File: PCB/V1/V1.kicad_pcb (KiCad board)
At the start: 2 copper layers, 19 parts, among them J2 Conn_01x01_Socket, J3 Conn_01x01_Socket, J4 Conn_01x01_Socket, J5 Conn_01x01_Socket, J7 Conn_01x01_Socket, J8 Conn_01x01_Socket, U1 ESP32-DEVKIT-V1, U2 L293D, U3 A4988_STEPPER_MOTOR_DRIVER_CA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, U5 YAAJ_DCDC_StepDown_LM2596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

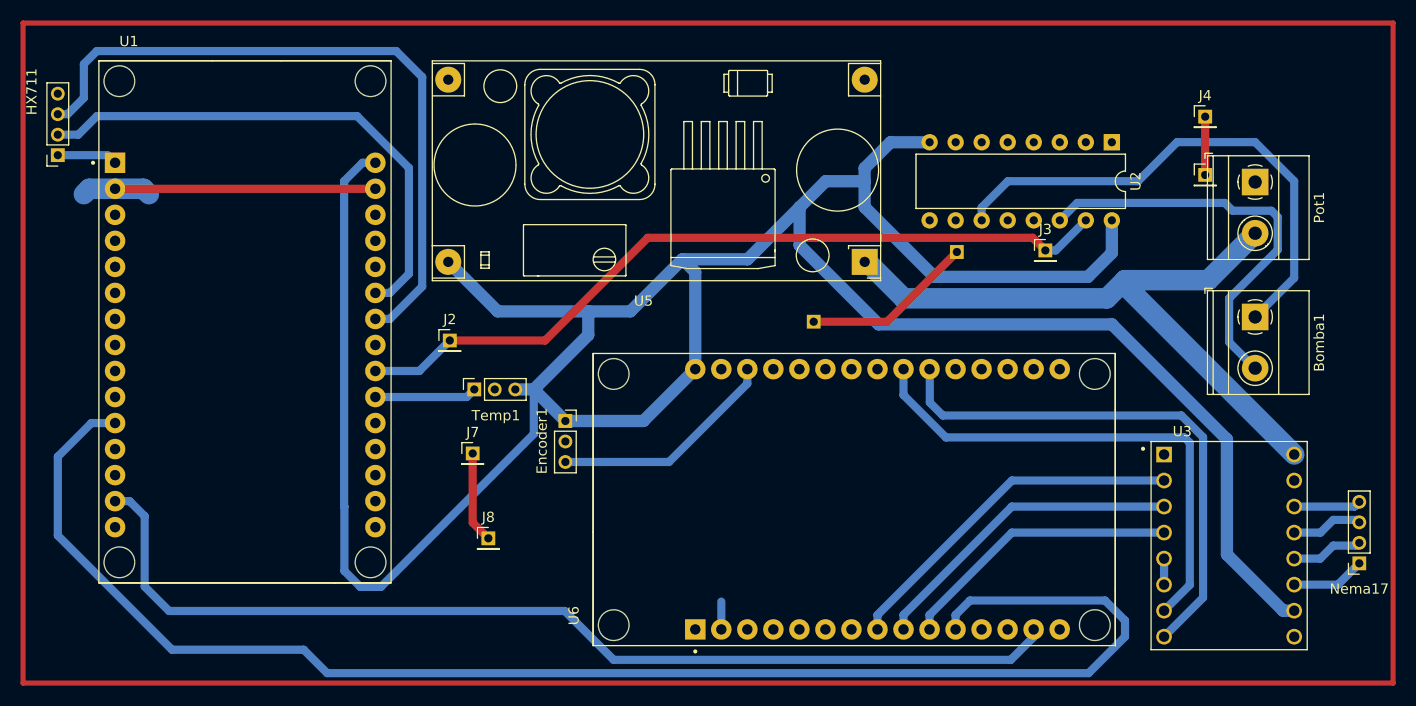
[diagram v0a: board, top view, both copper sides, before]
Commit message: pcb actualizada
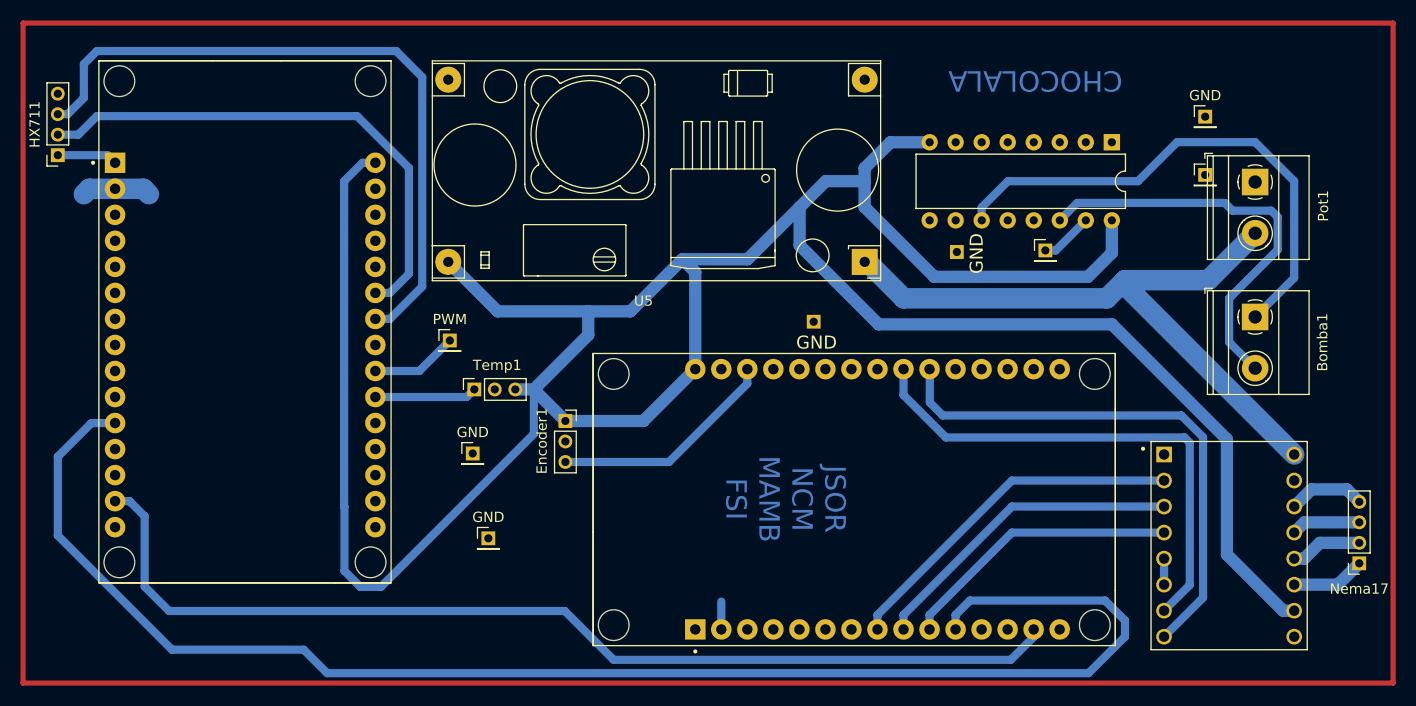
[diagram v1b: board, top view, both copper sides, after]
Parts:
- U3: value A4988_STEPPER_MOTOR_DRIVER_CARRIER -> A4988
- U5: value YAAJ_DCDC_StepDown_LM2596 -> LM2596
- gave numbers to parts that had none: 1
- renumbered J8 to GND, J4 to GND, J7 to GND, J2 to PWM
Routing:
- net PWM Bomba: track 76.4 -> 13.7 mm
- net GND: track 66.3 -> 9.51 mm
- net Net-(Nema17-Pin_4): track 6.54 -> 7.55 mm
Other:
- board text added: "JSOR NCM MAMB FSI"

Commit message: PCB implementada
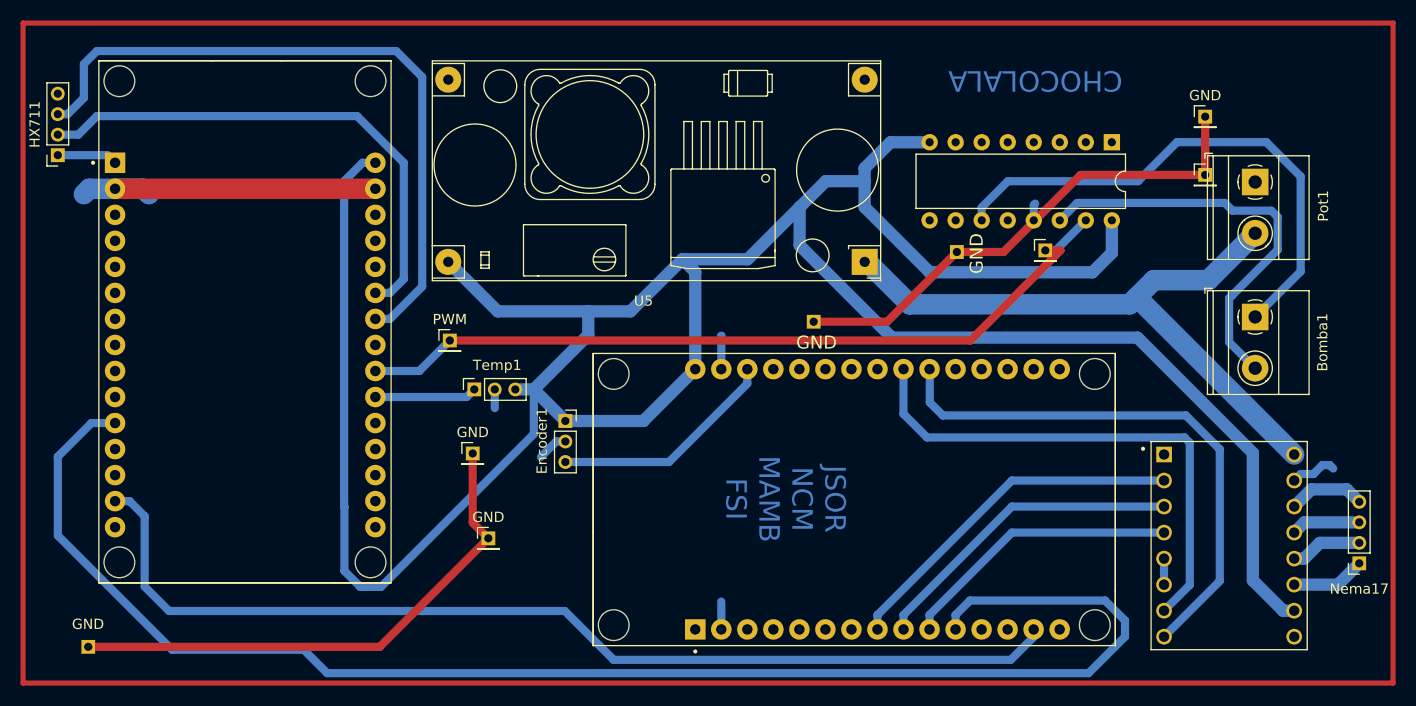
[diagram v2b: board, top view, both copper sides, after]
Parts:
- added ?: , , F.Cu at (94.4, 114.0)
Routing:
- net GND: track 9.51 -> 151.4 mm
- net PWM Bomba: track 13.7 -> 78.4 mm
- net 12V: track 65.8 -> 64.1 mm
- net Dir: track 52.3 -> 54.0 mm
- net Neg Bomba: track 50.8 -> 52.0 mm
- net Step: track 49.8 -> 50.9 mm
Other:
- board text added: "GND"
